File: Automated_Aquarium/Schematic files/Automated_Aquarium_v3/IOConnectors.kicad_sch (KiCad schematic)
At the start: 1 part, among them P1 USB_C_Plug

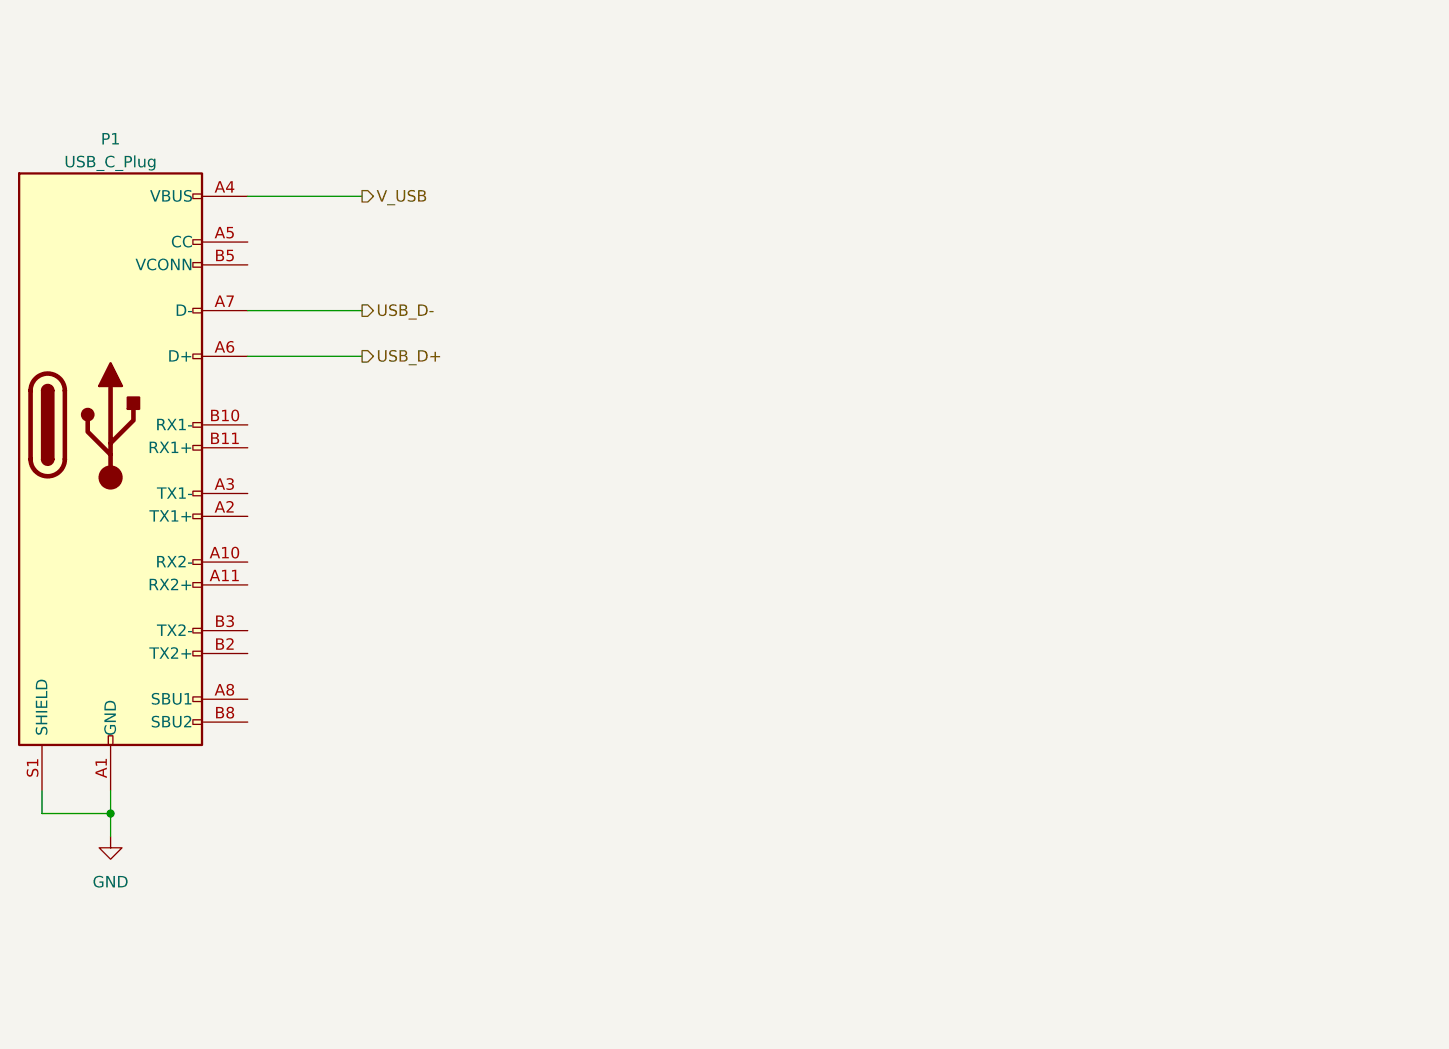
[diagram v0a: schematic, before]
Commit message: complete 0v1 layout aquarium
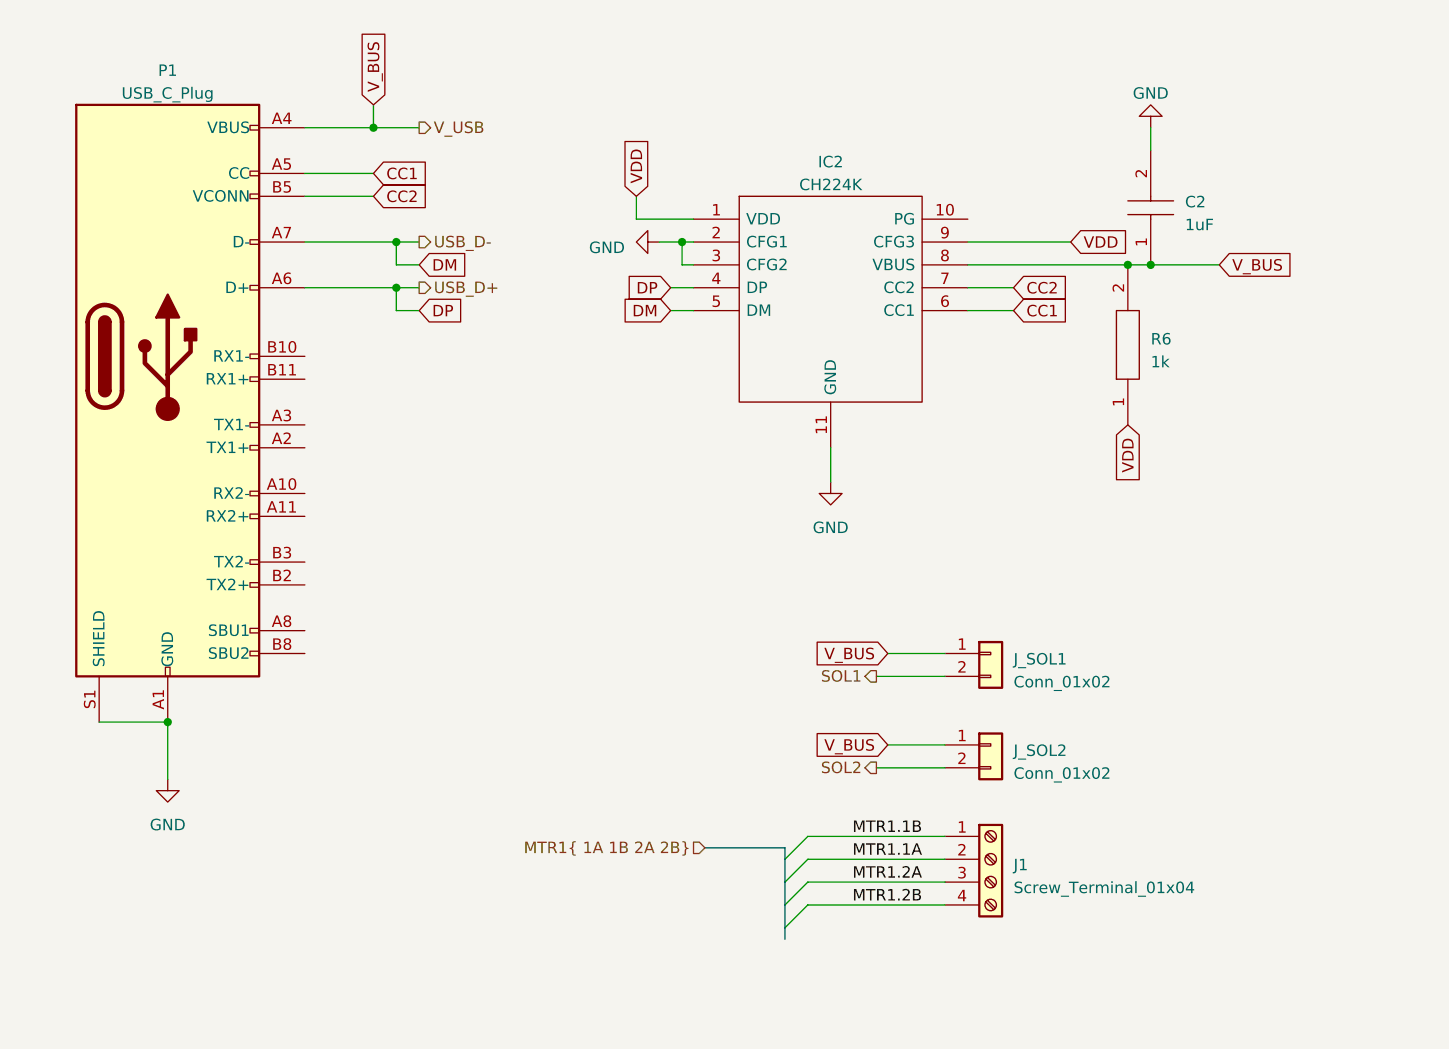
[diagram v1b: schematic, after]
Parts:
- added C2: 1uF, Capacitor_SMD:C_0603_1608Metric_Pad1.08x0.95mm_HandSolder, symbol SamacSys_Parts:0402B102K500NT
- added IC2: CH224K, SOP100P600X180-11N, symbol SamacSys_Parts:CH224K
- added J1: Screw_Terminal_01x04, symbol Connector:Screw_Terminal_01x04
- added J_SOL1, J_SOL2: Conn_01x02, Connector_PinHeader_2.54mm:PinHeader_1x02_P2.54mm_Vertical, symbol Connector_Generic:Conn_01x02
- added R6: 1k, RESC1608X55N, symbol SamacSys_Parts:RMCF0603ZT0R00
- P1: footprint digikey-footprints:USB-C_Female_E8124-015-01 -> Connector_USB:USB_C_Receptacle_GCT_USB4105-xx-A_16P_TopMnt_Horizontal; LCSC Part Number (none) -> C2982555
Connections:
- net GND: now also C2.2, IC2.11 (GND), IC2.2 (CFG1), IC2.3 (CFG2)
- net CC1: now reaches P1.A5 (CC)
- net CC1: now also IC2.6 (CC1)
- net CC2: now reaches P1.B5 (VCONN)
- net CC2: now also IC2.7 (CC2)
- net USB_D+ renamed DP
- net DP: now also IC2.4 (DP)
- net USB_D- renamed DM
- net DM: now also IC2.5 (DM)
- net V_USB renamed V_BUS
- net V_BUS: now also C2.1, IC2.8 (VBUS), J_SOL1.1 (Pin_1), J_SOL2.1 (Pin_1), R6.2
- new net MTR1.1A: J1.2 (Pin_2)
- new net MTR1.1B: J1.1 (Pin_1)
- new net MTR1.2A: J1.3 (Pin_3)
- new net MTR1.2B: J1.4 (Pin_4)
- new net SOL1: J_SOL1.2 (Pin_2)
- new net SOL2: J_SOL2.2 (Pin_2)
- new net VDD: IC2.1 (VDD), IC2.9 (CFG3), R6.1

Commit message: init pcb
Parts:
- removed J1: Screw_Terminal_01x04, symbol Connector:Screw_Terminal_01x04
- added J1, J2: Screw_Terminal_01x02, Connector_Phoenix_MC_HighVoltage:PhoenixContact_MCV_1,5_2-G-5.08_1x02_P5.08mm_Vertical, symbol Connector:Screw_Terminal_01x02
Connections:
- net MTR1.1A: now also J2.2 (Pin_2)
- net MTR1.1B: now also J2.1 (Pin_1)
- net MTR1.2A: now also J1.1 (Pin_1)
- net MTR1.2B: now also J1.2 (Pin_2)
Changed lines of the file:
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@@
     )
   )
-  (symbol (lib_id "Connector:Screw_Terminal_01x04") (at 186.69 130.81 0) (unit 1)
-    (in_bom yes) (on_board yes) (dnp no) (fields_autoplaced)
-    (property "Reference" "J1" (at 189.23 131.445 0)
-      (effects (font (size 1.27 1.27)) (justify left))
-    )
-    (property "Value" "Screw_Terminal_01x04" (at 189.23 133.985 0)
-      (effects (font (size 1.27 1.27)) (justify left))
-    )
-    (property "Footprint" "" (at 186.69 130.81 0)
-      (effects (font (size 1.27 1.27)) hide)
-    )
-    (property "Datasheet" "~" (at 186.69 130.81 0)
-      (effects (font (size 1.27 1.27)) hide)
-    )
-    (pin "1")
-    (pin "2")
-    (pin "3")
-    (pin "4")
-    (instances
-      (project "Automated_Aquarium_v3"
-        (path "/953ef1f2-1b30-471f-8352-2e2b084ebc55/776c66f3-b8e4-46d2-a967-edc0306303b2"
-          (reference "J1") (unit 1)
+  (symbol (lib_id "Connector:Screw_Terminal_01x02") (at 186.69 128.27 0) (unit 1)
+    (in_bom yes) (on_board yes) (dnp no) (fields_autoplaced)
+    (property "Reference" "J2" (at 189.23 128.905 0)
+      (effects (font (size 1.27 1.27)) (justify left))
+    )
+    (property "Value" "Screw_Terminal_01x02" (at 189.23 131.445 0)
+      (effects (font (size 1.27 1.27)) (justify left))
+    )
+    (property "Footprint" "Connector_Phoenix_MC_HighVoltage:PhoenixContact_MCV_1,5_2-G-5.08_1x02_P5.08mm_Vertical" (at 186.69 128.27 0)
+      (effects (font (size 1.27 1.27)) hide)
+    )
+    (property "Datasheet" "~" (at 186.69 128.27 0)
+      (effects (font (size 1.27 1.27)) hide)
+    )
+    (property "LCSC Part Number" "C8269" (at 186.69 128.27 0)
+      (effects (font (size 1.27 1.27)) hide)
+    )
+    (pin "1")
+    (pin "2")
+    (instances
+      (project "Automated_Aquarium_v3"
+        (path "/953ef1f2-1b30-471f-8352-2e2b084ebc55/776c66f3-b8e4-46d2-a967-edc0306303b2"
+          (reference "J2") (unit 1)
         )
       )
@@
         )
       )
+    )
+  )
+  (symbol (lib_id "Connector:Screw_Terminal_01x02") (at 186.69 133.35 0) (unit 1)
+    (in_bom yes) (on_board yes) (dnp no) (fields_autoplaced)
+    (property "Reference" "J1" (at 189.23 133.985 0)
+      (effects (font (size 1.27 1.27)) (justify left))
+    )
+    (property "Value" "Screw_Terminal_01x02" (at 189.23 136.525 0)
+      (effects (font (size 1.27 1.27)) (justify left))
+    )
+    (property "Footprint" "Connector_Phoenix_MC_HighVoltage:PhoenixContact_MCV_1,5_2-G-5.08_1x02_P5.08mm_Vertical" (at 186.69 133.35 0)
+      (effects (font (size 1.27 1.27)) hide)
+    )
+    (property "Datasheet" "~" (at 186.69 133.35 0)
+      (effects (font (size 1.27 1.27)) hide)
+    )
+    (property "LCSC Part Number" "C8269" (at 186.69 133.35 0)
+      (effects (font (size 1.27 1.27)) hide)
+    )
+    (pin "1")
+    (pin "2")
+    (instances
+      (project "Automated_Aquarium_v3"
+        (path "/953ef1f2-1b30-471f-8352-2e2b084ebc55/776c66f3-b8e4-46d2-a967-edc0306303b2"
+          (reference "J1") (unit 1)
+        )
+      )

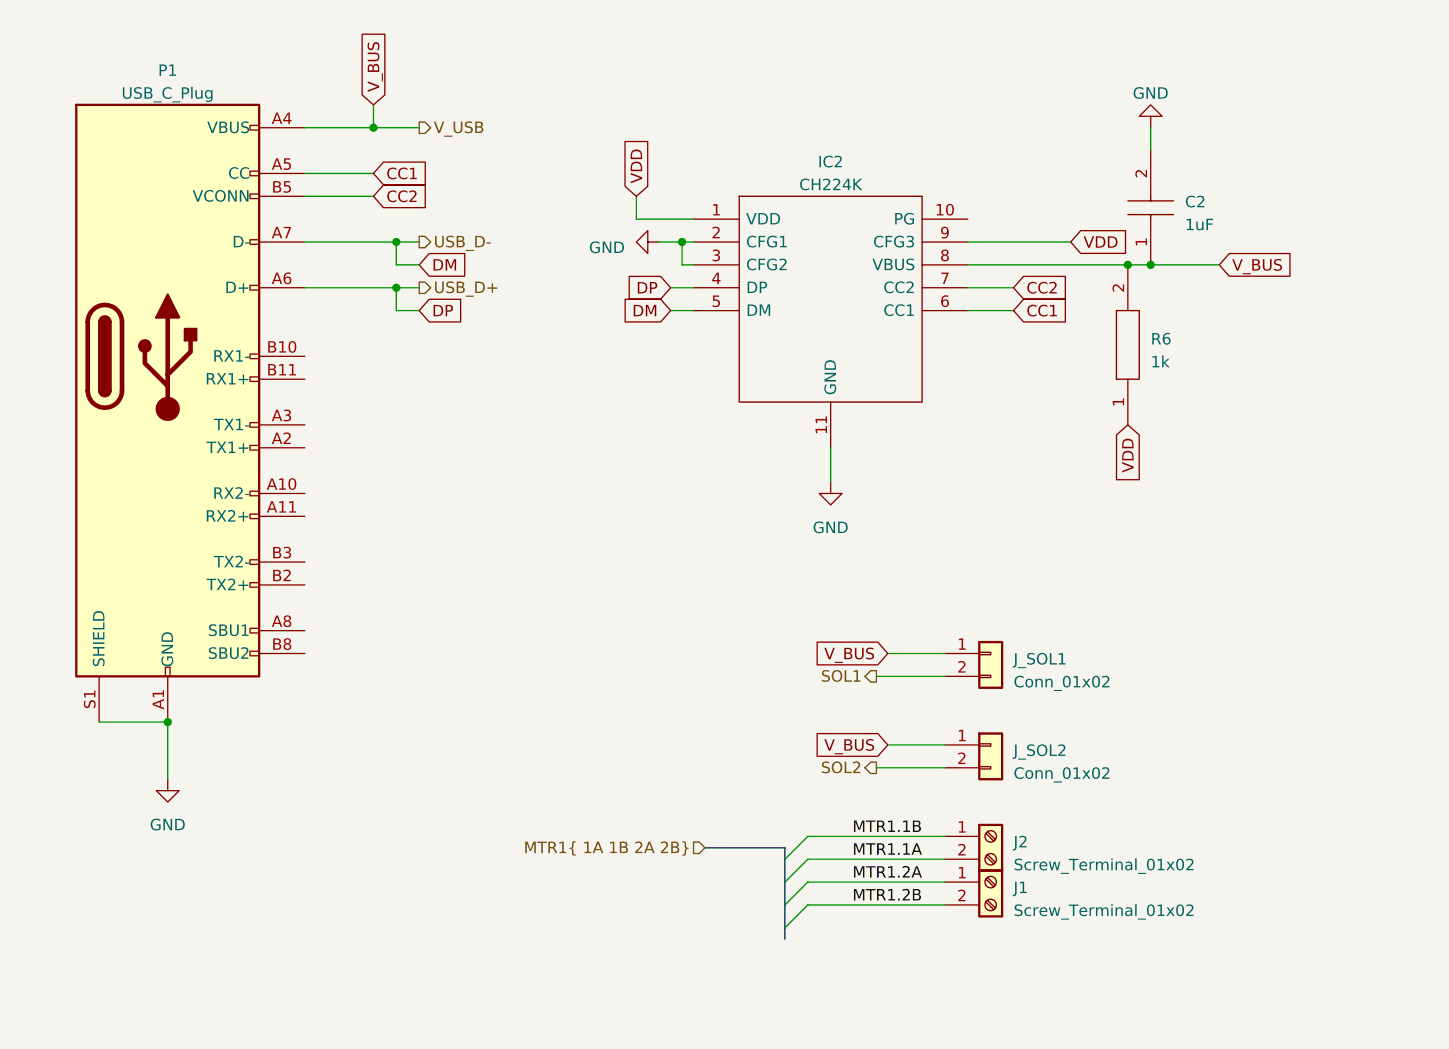
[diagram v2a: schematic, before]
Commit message: finish aqua schem, add inital layout
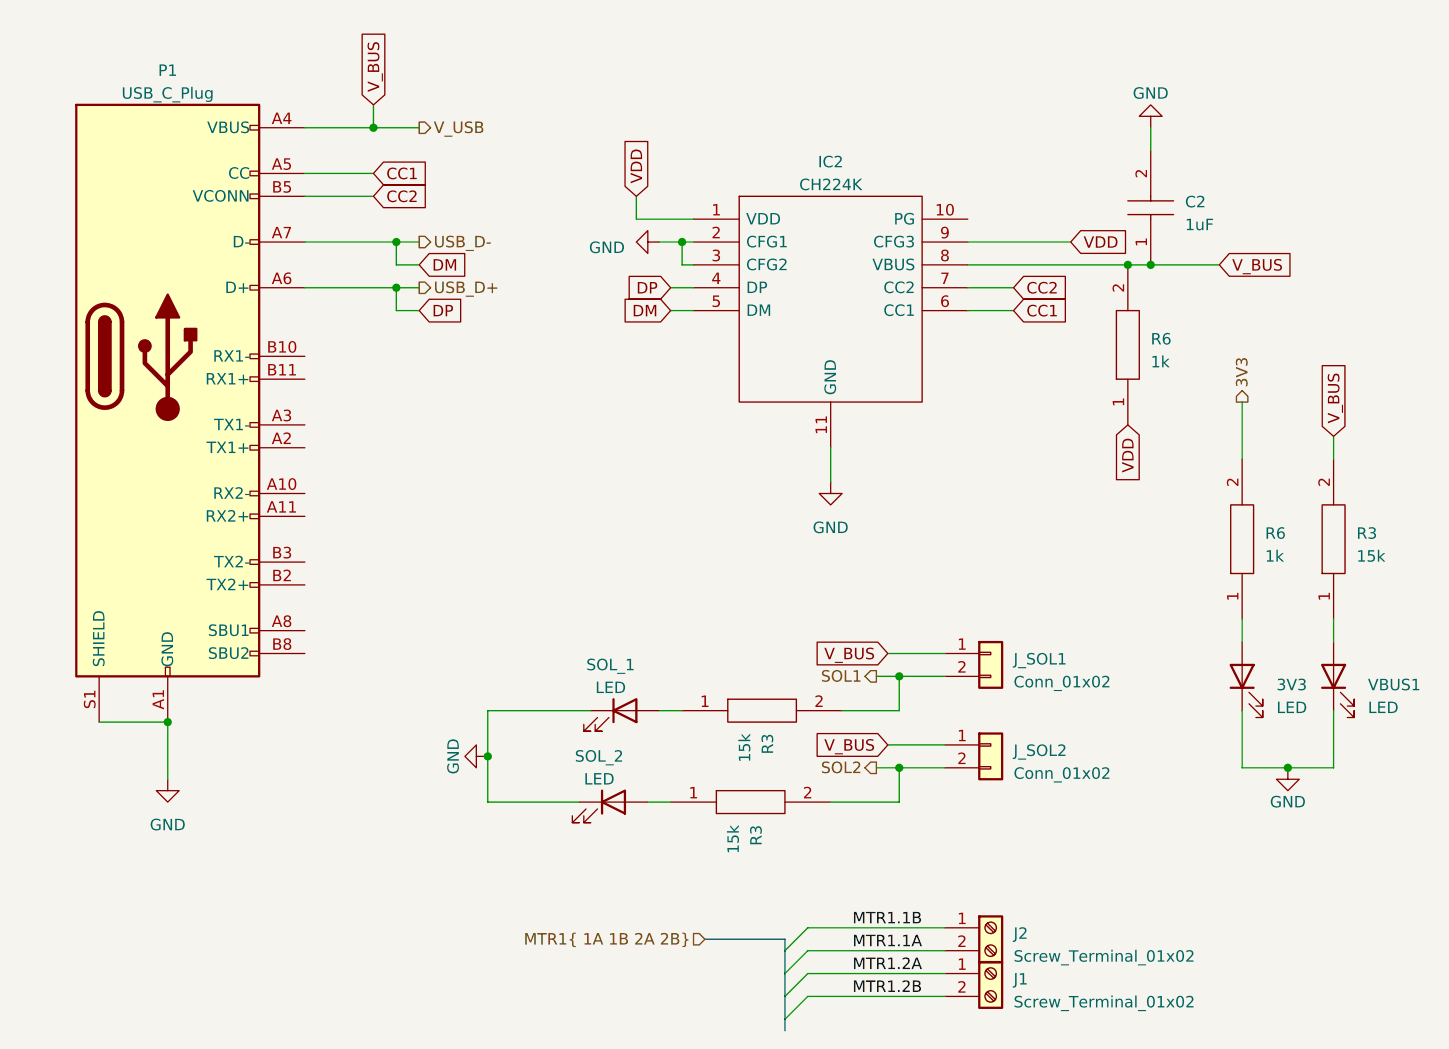
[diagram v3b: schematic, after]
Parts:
- added 3V3, SOL_1, SOL_2, VBUS1: LED, LED_SMD:LED_0603_1608Metric_Pad1.05x0.95mm_HandSolder, symbol Device:LED
- added R3 (x3): 15k, RESC1608X55N, symbol SamacSys_Parts:RMCF0603ZT0R00
- added R6: 1k, RESC1608X55N, symbol SamacSys_Parts:RMCF0603ZT0R00
- C2: LCSC Part Number C15849 -> C377755
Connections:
- net GND: now also 3V3.1 (K), SOL_1.1 (K), SOL_2.1 (K), VBUS1.1 (K)
- net SOL1: now also R3.2
- net SOL2: now also R3.2
- net V_BUS: now also R3.2
- new net: R3.1, SOL_1.2 (A)
- new net: R3.1, SOL_2.2 (A)
- new net: R3.1, VBUS1.2 (A)
- new net: 3V3.2 (A), R6.1
- new net 3V3: R6.2
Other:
- moved on the sheet: J1, J2
